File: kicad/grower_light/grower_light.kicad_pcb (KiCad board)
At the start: 2 copper layers, 14 parts, among them J1 Conn_01x06, J2 Temp, J3 Light, U1 ATMEGA328PB-AU, Y1 9,216 MHz

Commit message: Add source and update schematic
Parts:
- added C7: 100n, Capacitor_SMD:C_0805_2012Metric, F.Cu at (166.1, 100.9)
- added C8: 100n, Capacitor_SMD:C_0805_2012Metric, F.Cu at (161.8, 100.9)
- added J4: AVR_UART, Connector_PinHeader_2.54mm:PinHeader_1x03_P2.54mm_Vertical, F.Cu at (158.8, 64.8)
- added J5: ESP_UART, Connector_PinHeader_2.54mm:PinHeader_1x03_P2.54mm_Vertical, F.Cu at (166.5, 64.8)
- added L1: 100u, Inductor_SMD:L_0805_2012Metric, F.Cu at (157.5, 100.9)
- added U2: ESP-12_07v2, lib:ESP-07v2, F.Cu at (176.4, 87.8)
- U1: value ATMEGA328PB-AU -> ATMEGA328-AU
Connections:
- U1 pad 18: VCC -> Net-(C7-Pad2)
- U1 pad 3: Net-(U1-Pad3) -> GND
- U1 pad 6: Net-(U1-Pad6) -> VCC

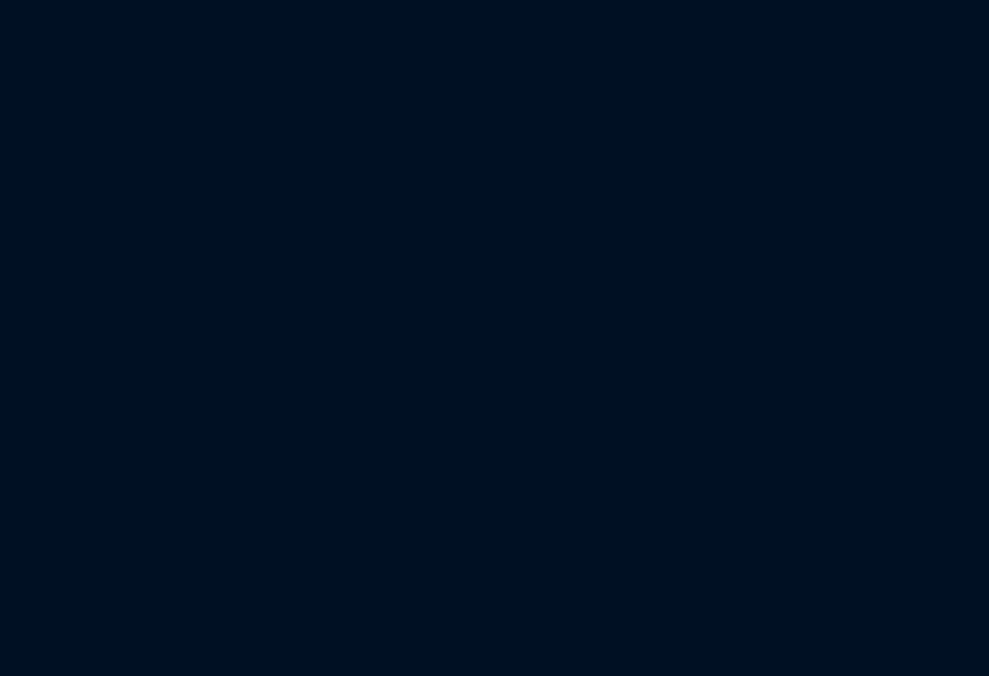
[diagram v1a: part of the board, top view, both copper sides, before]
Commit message: Add ds1307 clock
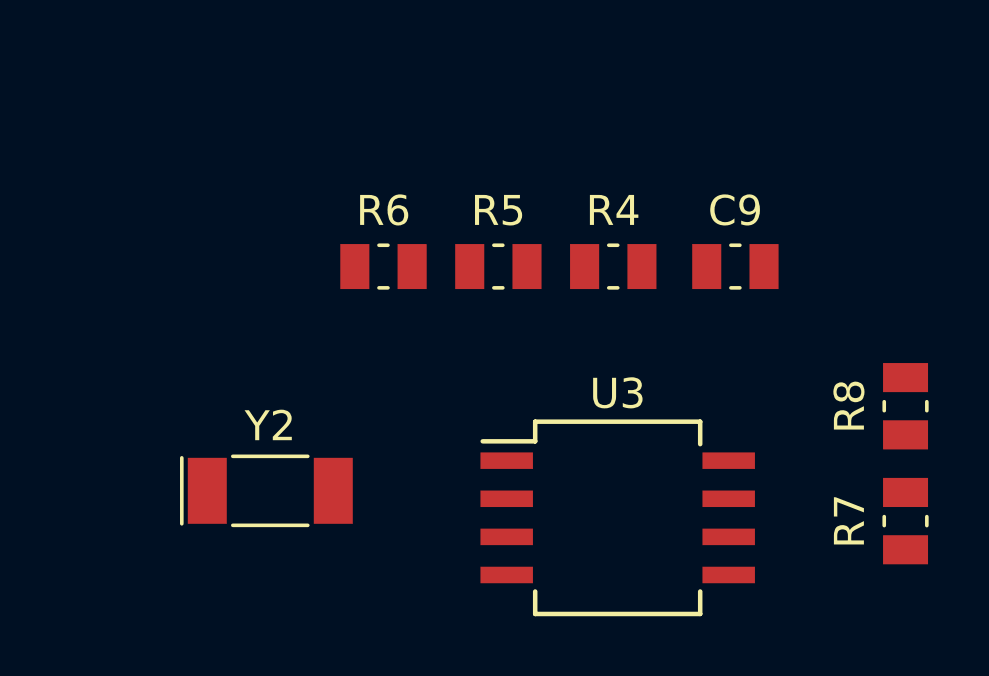
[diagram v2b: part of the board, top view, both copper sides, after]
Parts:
- added C9: 100n, Capacitor_SMD:C_0805_2012Metric, F.Cu at (188.5, 111.5)
- added R4: 100, Resistor_SMD:R_0805_2012Metric, F.Cu at (184.5, 111.5)
- added R5: 10k, Resistor_SMD:R_0805_2012Metric, F.Cu at (180.6, 111.5)
- added R6: 10k, Resistor_SMD:R_0805_2012Metric, F.Cu at (176.8, 111.5)
- added R7: 4k7, Resistor_SMD:R_0805_2012Metric, F.Cu at (194.2, 120.0)
- added R8: 4k7, Resistor_SMD:R_0805_2012Metric, F.Cu at (194.2, 116.2)
- added U3: DS1307Z+, Package_SOIC:SO-8_5.3x6.2mm_P1.27mm, F.Cu at (184.6, 119.9)
- added Y2: 32768, Crystal:Crystal_SMD_MicroCrystal_CC4V-T1A-2Pin_5.0x1.9mm, F.Cu at (173.0, 119.0)
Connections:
- U1 pad 27: Net-(U1-Pad27) -> /SDA
- U1 pad 28: Net-(U1-Pad28) -> /SCL
- U2 pad 15: /TX -> /RX
- U2 pad 16: /RX -> /TX

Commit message: Start work with pcb
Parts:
- C1, C2, C3, C4, C5, C6, C7, C8, C9, L1, R1, R2, R3, R4, R5, R6, R7, R8, U1, U2, U3, Y2: moved to B.Cu
- J1: value Conn_01x06 -> AVR_ISP
- moved C9 117.9 mm to (71.1, 100.7), turned to 90 degrees
- moved R4 114.0 mm to (72.1, 92.1), turned to 180 degrees
- moved R6 106.8 mm to (71.1, 96.2), turned to 90 degrees
- moved C6 93.7 mm to (73.0, 79.7), turned to 270 degrees
- moved U2 90.1 mm to (86.4, 90.2)
- moved R5 86.0 mm to (98.7, 85.1), turned to 180 degrees
- moved R7 85.3 mm to (111.1, 100.6)
- moved R8 83.9 mm to (111.1, 104.5), turned to 270 degrees
- moved J5 74.2 mm to (102.9, 102.9), turned to 180 degrees
- moved U3 69.0 mm to (118.1, 101.6), turned to 180 degrees
- moved C4 66.0 mm to (99.7, 80.3), turned to 90 degrees
- moved J4 64.6 mm to (106.7, 102.9), turned to 180 degrees
- moved Y2 49.1 mm to (127.0, 101.8), turned to 90 degrees
- moved C5 48.0 mm to (131.8, 80.0), turned to 180 degrees
- moved C1 44.7 mm to (109.9, 86.5), turned to 90 degrees
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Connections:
- net Net-(C7-Pad2) renamed /AVCC
- net Net-(C8-Pad2) renamed /AREF
- net Net-(C9-Pad2) renamed /RES_ESP
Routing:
- net GND: track 0.00 -> 288.0 mm
- net VCC: track 0.00 -> 162.9 mm
- net /TEMP: track 0.00 -> 40.6 mm
- net /RES: track 0.00 -> 34.3 mm
- net /LIGHT: track 0.00 -> 32.0 mm
- net Net-(C2-Pad2): track 0.00 -> 22.8 mm
- net /SDA: track 0.00 -> 18.1 mm
- net Net-(J4-Pad1): track 0.00 -> 18.1 mm
- net /SCL: track 0.00 -> 16.8 mm
- net /MOSI: track 0.00 -> 14.8 mm
- net Net-(J4-Pad2): track 0.00 -> 14.2 mm
- net /TX: track 0.00 -> 11.6 mm
- net /RX: track 0.00 -> 11.5 mm
- net /AVCC: track 0.00 -> 10.4 mm
- net /SCK: track 0.00 -> 9.83 mm
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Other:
- net class Default: clearance 0.2 -> 0.1
- rule trace_clearance: 0.2 -> 0.1

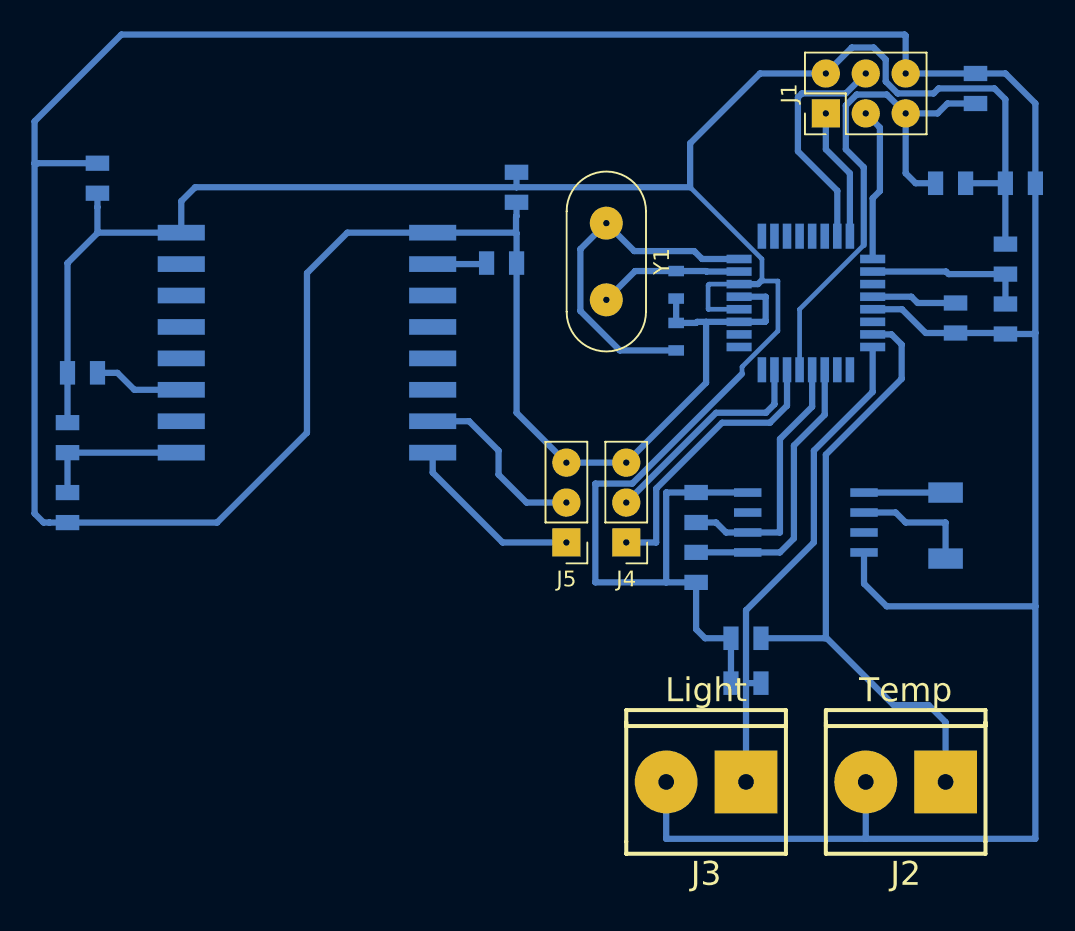
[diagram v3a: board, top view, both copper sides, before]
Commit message: Create server witch cfg
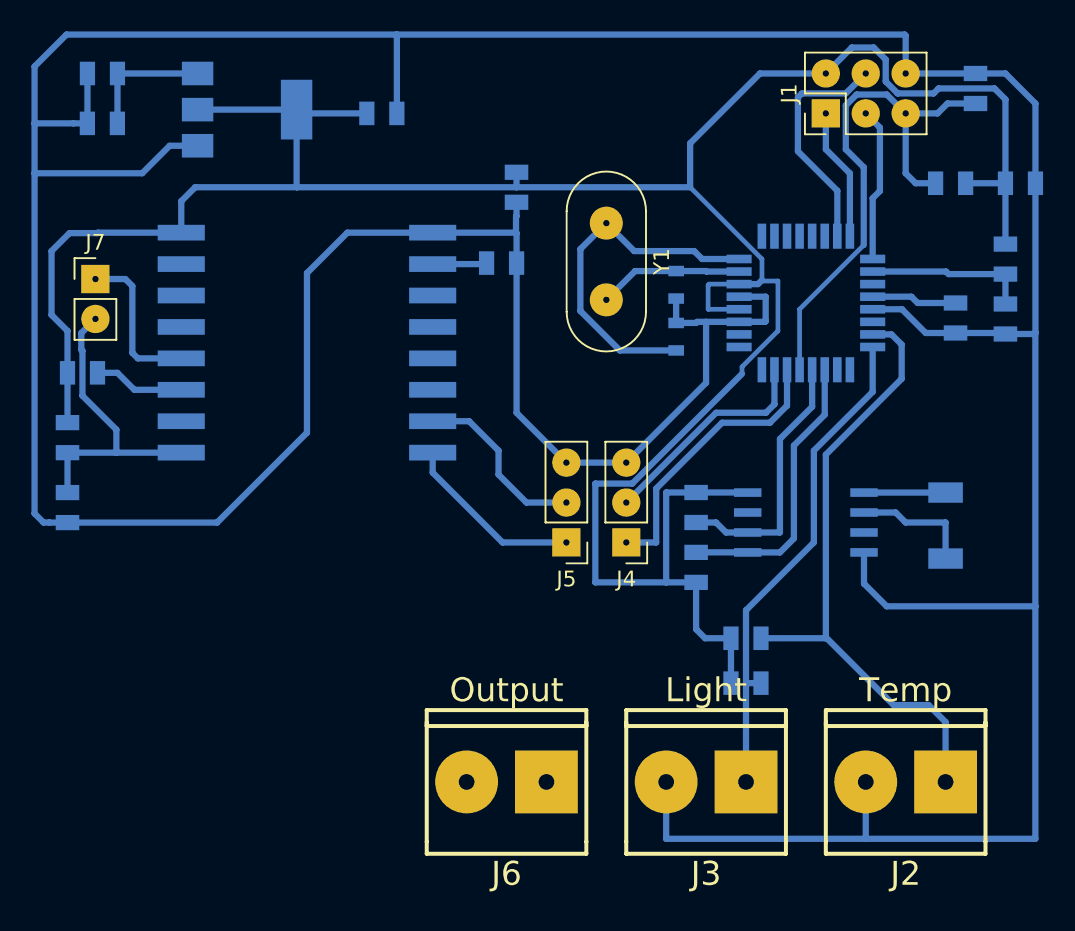
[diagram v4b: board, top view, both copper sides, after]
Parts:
- added C10: 100n, Capacitor_SMD:C_0805_2012Metric, B.Cu at (91.1, 75.6)
- added C11: 100n, Capacitor_SMD:C_0805_2012Metric, B.Cu at (131.8, 80.0)
- added J6: Output, w_conn_screw:mors_2p, F.Cu at (99.1, 118.1)
- added J7: Sleep, Connector_PinHeader_2.54mm:PinHeader_1x02_P2.54mm_Vertical, F.Cu at (72.9, 86.1)
- added U4: LD1117S33TR_SOT223, Package_TO_SOT_SMD:SOT-223-3_TabPin2, B.Cu at (82.5, 75.3)
- moved C5 58.8 mm to (73.3, 73.0), turned to 0 degrees
- moved C6 3.50 mm to (73.3, 76.2), turned to 0 degrees
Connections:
- C5 pad 2: VCC -> +5V
- C6 pad 2: VCC -> +5V
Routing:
- net GND: track 288.0 -> 308.8 mm
- net VCC: track 162.9 -> 178.1 mm
- net Net-(J7-Pad1): track 0.00 -> 10.0 mm
- net /RES_ESP: track 9.78 -> 19.6 mm
- net +5V: track 0.00 -> 8.28 mm

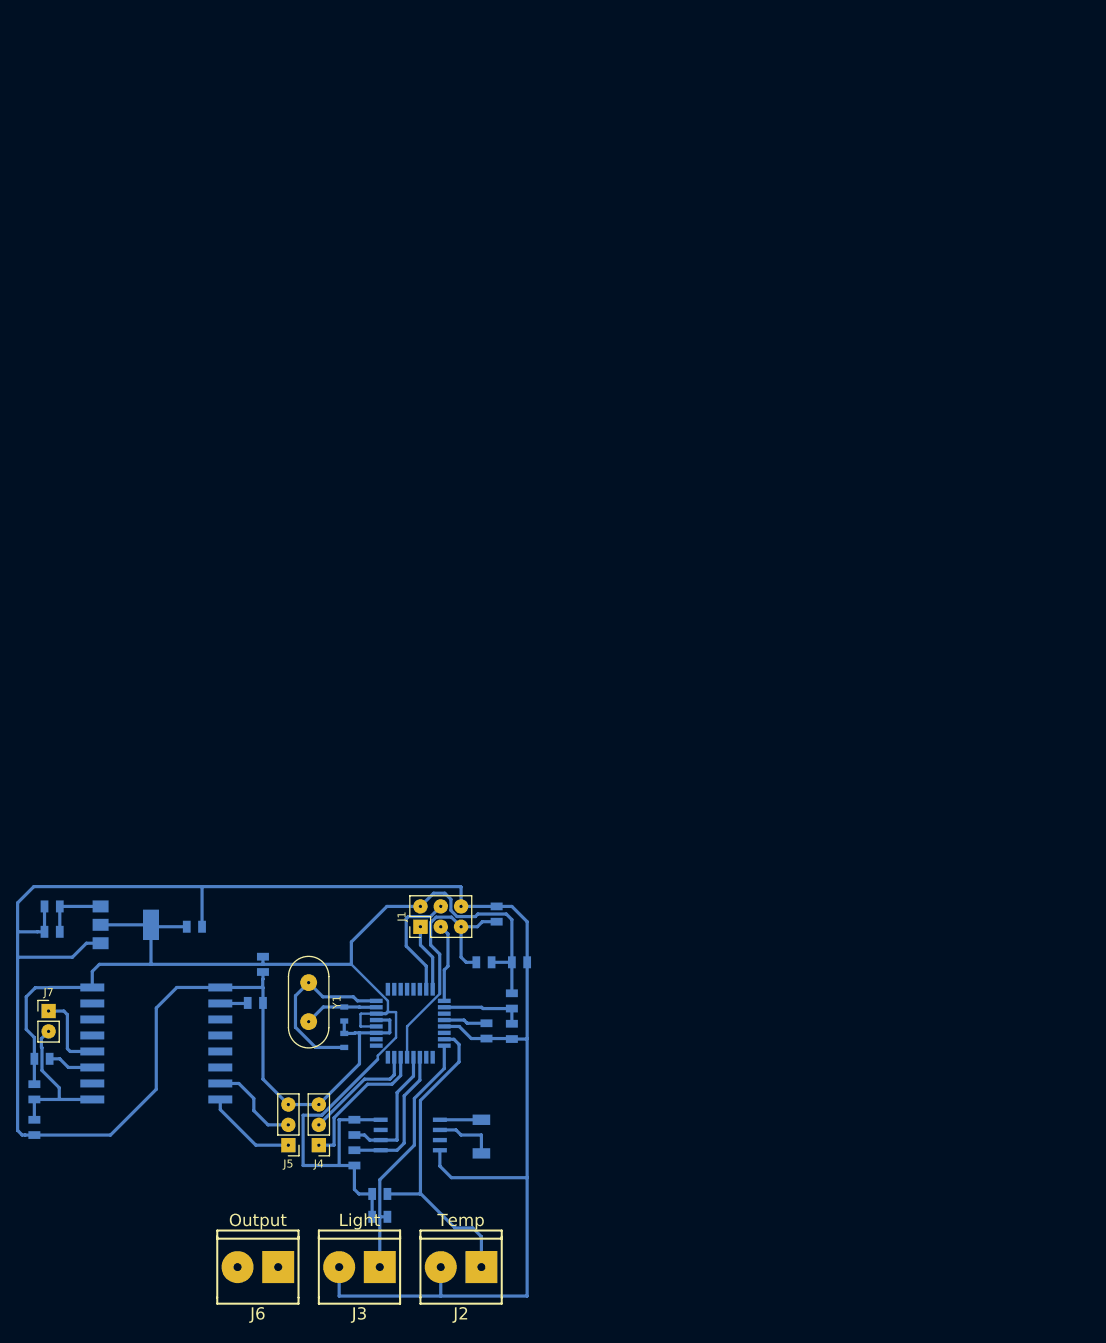
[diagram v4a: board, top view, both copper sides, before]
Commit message: Change schematic for only esp8266
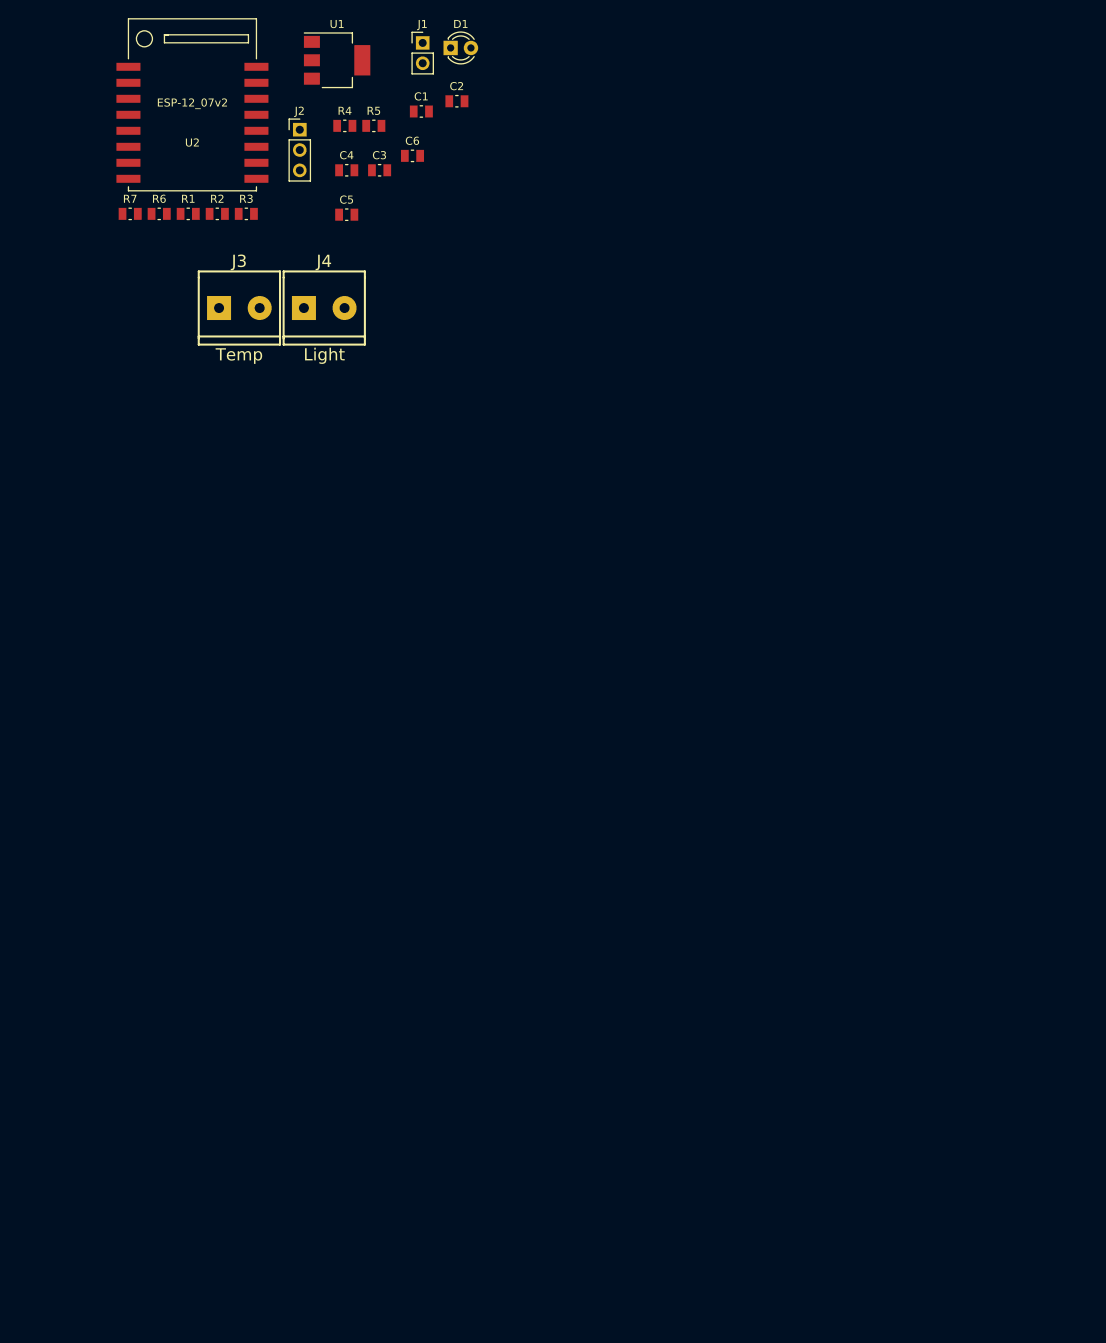
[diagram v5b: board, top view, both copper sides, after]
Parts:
- removed C10, C11, C7, C8, C9: 100n, Capacitor_SMD:C_0805_2012Metric
- removed J5: ESP_UART, Connector_PinHeader_2.54mm:PinHeader_1x03_P2.54mm_Vertical
- removed J6: Output, w_conn_screw:mors_2p
- removed J7: Sleep, Connector_PinHeader_2.54mm:PinHeader_1x02_P2.54mm_Vertical
- removed L1: 100u, Inductor_SMD:L_0805_2012Metric
- removed R8: 4k7, Resistor_SMD:R_0805_2012Metric
- removed U3: DS1307Z+, Package_SOIC:SO-8_5.3x6.2mm_P1.27mm
- removed U4: LD1117S33TR_SOT223, Package_TO_SOT_SMD:SOT-223-3_TabPin2
- removed Y1: 9,216 MHz, Crystal:Crystal_HC49-4H_Vertical
- removed Y2: 32768, Crystal:Crystal_SMD_MicroCrystal_CC4V-T1A-2Pin_5.0x1.9mm
- added D1: LED, LED_THT:LED_D3.0mm, F.Cu at (123.2, -34.3)
- C1, C2: value 22p -> 100n; footprint Capacitor_SMD:C_0603_1608Metric -> Capacitor_SMD:C_0805_2012Metric; moved to F.Cu
- C3, C4, C5, C6, R1, R4, U2: moved to F.Cu
- J1: value AVR_ISP -> Sleep; footprint Connector_PinHeader_2.54mm:PinHeader_2x03_P2.54mm_Vertical -> Connector_PinHeader_2.54mm:PinHeader_1x02_P2.54mm_Vertical
- J2: value Temp -> ESP_UART; footprint w_conn_screw:mors_2p -> Connector_PinHeader_2.54mm:PinHeader_1x03_P2.54mm_Vertical
- J3: value Light -> Temp
- J4: value AVR_UART -> Light; footprint Connector_PinHeader_2.54mm:PinHeader_1x03_P2.54mm_Vertical -> w_conn_screw:mors_2p
- R2: value 1k -> 27k; moved to F.Cu
- R3: value 10k -> 1k; moved to F.Cu
- R5: value 10k -> 12k; moved to F.Cu
- R6: value 10k -> 220; moved to F.Cu
- R7: value 4k7 -> 10k; moved to F.Cu
- U1: value ATMEGA328-AU -> LD1117S33TR_SOT223; footprint Package_QFP:TQFP-32_7x7mm_P0.8mm -> Package_TO_SOT_SMD:SOT-223-3_TabPin2; moved to F.Cu
- moved J2 143.6 mm to (104.3, -24.1), turned to 0 degrees
- moved R3 126.5 mm to (97.6, -13.5), turned to 0 degrees
- moved R2 124.2 mm to (94.0, -13.5), turned to 0 degrees
- moved R4 122.6 mm to (109.9, -24.5), turned to 0 degrees
- moved J3 120.8 mm to (96.7, -1.77), turned to 0 degrees
- moved U1 120.7 mm to (109.0, -32.7)
- moved C2 118.2 mm to (123.9, -27.6), turned to 0 degrees
- moved R7 117.6 mm to (83.1, -13.5), turned to 0 degrees
- moved U2 115.2 mm to (90.9, -24.9)
- moved C1 113.2 mm to (119.5, -26.3), turned to 0 degrees
- moved R6 110.8 mm to (86.7, -13.5), turned to 0 degrees
- moved R5 110.6 mm to (113.6, -24.5), turned to 0 degrees
- moved J1 110.5 mm to (119.7, -34.9), turned to 0 degrees
- moved C6 106.9 mm to (118.4, -20.8)
- moved J4 104.6 mm to (107.4, -1.77), turned to 0 degrees
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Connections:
- net Net-(U2-Pad14) renamed /OUT
- C1 pad 2: Net-(C1-Pad2) -> +5V
- C2 pad 2: Net-(C2-Pad2) -> +5V
- C3 pad 2: /RES -> VCC
- C5 pad 2: +5V -> VCC
- C6 pad 2: +5V -> /RES_ESP
- J1 pad 1: /MISO -> Net-(J1-Pad1)
- J1 pad 2: VCC -> /RES_ESP
- J2 pad 1: /TEMP -> /TX
- J2 pad 2: GND -> /RX
- J3 pad 1: /LIGHT -> /ADC
- J3 pad 2: GND -> /ML
- J4 pad 1: Net-(J4-Pad1) -> /ADC
- J4 pad 2: Net-(J4-Pad2) -> /MT
- R1 pad 1: /RES -> /RES_ESP
- R2 pad 1: /TEMP -> /ADC
- R2 pad 2: VCC -> /MLP
- R3 pad 1: /LIGHT -> /ADC
- R3 pad 2: VCC -> /MTP
- R5 pad 1: GND -> /ML
- R5 pad 2: Net-(R5-Pad2) -> /ADC
- R6 pad 1: /RES_ESP -> Net-(D1-Pad2)
- R6 pad 2: VCC -> /LED
- R7 pad 1: /SCL -> GND
- R7 pad 2: VCC -> Net-(R7-Pad2)
- U1 pad 1: Net-(U1-Pad1) -> GND
- U1 pad 2: Net-(U1-Pad2) -> VCC
- U1 pad 3: GND -> +5V
- U2 pad 10: Net-(R5-Pad2) -> Net-(R7-Pad2)
- U2 pad 11: Net-(U2-Pad11) -> /LED
- U2 pad 13: Net-(U2-Pad13) -> /MTP
- U2 pad 2: Net-(U2-Pad2) -> /ADC
- U2 pad 4: Net-(J7-Pad1) -> Net-(J1-Pad1)
- U2 pad 5: Net-(U2-Pad5) -> /MT
- U2 pad 6: Net-(U2-Pad6) -> /ML
- U2 pad 7: Net-(U2-Pad7) -> /MLP
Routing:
- net GND: track 308.8 -> 0.00 mm
- net VCC: track 178.1 -> 0.00 mm
- net /TEMP: track 40.6 -> 0.00 mm
- net /RES: track 34.3 -> 0.00 mm
- net /LIGHT: track 32.0 -> 0.00 mm
- net Net-(C2-Pad2): track 22.8 -> 0.00 mm
- net /RES_ESP: track 19.6 -> 0.00 mm
- net /SDA: track 18.1 -> 0.00 mm
- net Net-(J4-Pad1): track 18.1 -> 0.00 mm
- net /SCL: track 16.8 -> 0.00 mm
- net /MOSI: track 14.8 -> 0.00 mm
- net Net-(J4-Pad2): track 14.2 -> 0.00 mm
- net /TX: track 11.6 -> 0.00 mm
- net /RX: track 11.5 -> 0.00 mm
- net /AVCC: track 10.4 -> 0.00 mm
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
